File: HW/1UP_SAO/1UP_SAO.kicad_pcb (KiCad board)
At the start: 2 copper layers, 48 x 48 mm, 17 parts, among them X1 Badgelife_sao_connector_v169b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

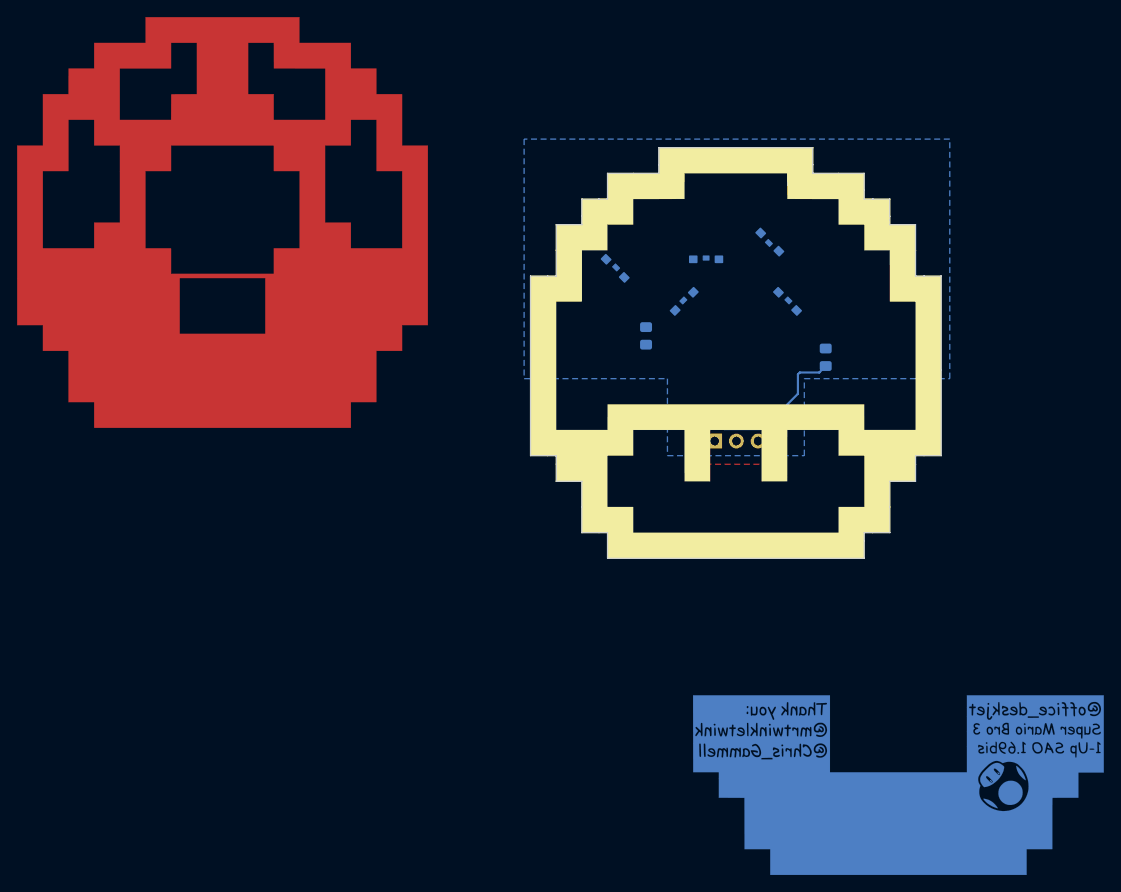
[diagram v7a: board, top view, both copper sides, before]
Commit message: all placements done, TODO: test gerbs
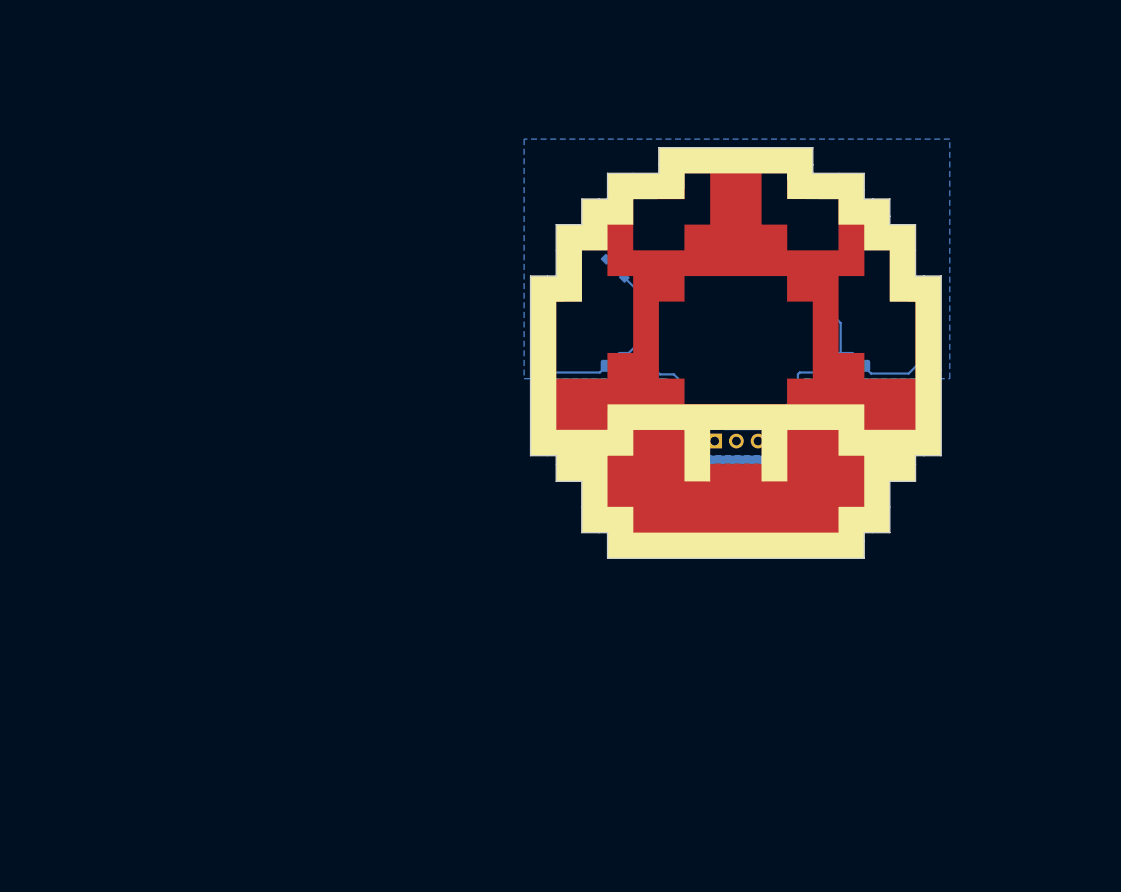
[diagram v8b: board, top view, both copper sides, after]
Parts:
- moved G*** 61.9 mm to (100.0, 100.0)
- moved G*** 41.6 mm to (100.0, 100.0)
- moved D2 5.86 mm to (90.2, 98.5), turned to 90 degrees
- moved D7 5.86 mm to (109.8, 98.5), turned to 270 degrees
- moved R1 5.09 mm to (85.8, 101.5), turned to 180 degrees
- moved R2 3.74 mm to (114.1, 101.5), turned to 0 degrees
- moved D8 3.67 mm to (100.0, 90.2)
- moved D1 0.32 mm to (91.2, 81.2)
- moved D4 0.25 mm to (78.2, 98.5)
- moved D5 0.25 mm to (104.2, 87.0)
- moved D6 0.25 mm to (121.8, 97.0)
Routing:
- net Net-(D1-Pad2): track 0.00 -> 45.0 mm
- net Net-(D5-Pad2): track 0.00 -> 37.9 mm
- net VCC: track 17.8 -> 35.0 mm
